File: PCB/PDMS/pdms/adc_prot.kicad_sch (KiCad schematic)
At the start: 20 parts

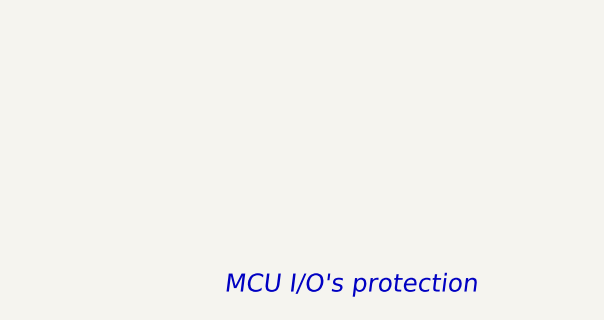
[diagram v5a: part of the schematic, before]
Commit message: WIP PCB folder structure and schematic clean-up
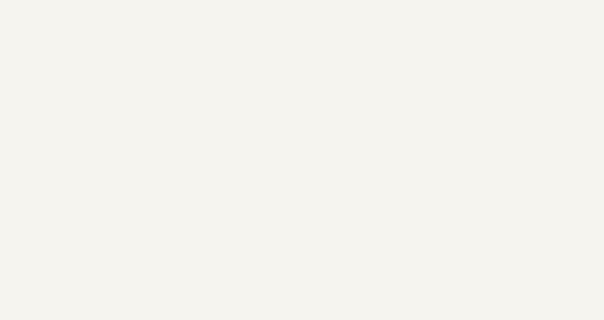
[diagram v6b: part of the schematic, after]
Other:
- note removed: "MCU I/O's protection"
- company: (none) -> PGRacing Team
- title: (none) -> MCU I/O's protection
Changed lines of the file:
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@@
 (kicad_sch (version 20211123) (generator eeschema)
   (paper "A4")
+  (title_block
+    (title "MCU I/O's protection")
+    (rev "V4.2")
+    (company "PGRacing Team")
+    (comment 1 "Karol Pergoł")
+  )
   (junction (at 125.603 107.696) (diameter 0) (color 0 0 0 0)
   )
@@
     (stroke (width 0) (type default) (color 0 0 0 0))
   )
-  (text "MCU I/O's protection" (at 186.182 191.008 0)
-    (effects (font (size 2 2) italic) (justify left bottom))
-  )
   (label "ADC_IN7" (at 106.553 129.794 0)

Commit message: PDMS PCB input modification WIP - no supply
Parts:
- added C102, C89, C96, C97: 100nF, Resistor_SMD:R_0402_1005Metric, symbol Device:C_Small
- added C32, C33, C34, C35, C36, C37, C38, C39: 47nF, Capacitor_SMD:C_0402_1005Metric, symbol Device:C_Small
- added D55, D56, D57, D58: TSD05, Diode_SMD:D_SOD-323, symbol Device:D_TVS
- added D63, D64, D65, D66: SZMM5Z5V3, Diode_SMD:D_SOD-523, symbol Device:D_Zener_Small
- added R125, R126, R129, R130, R133, R134, R135, R136: 1k/0.2W, Resistor_SMD:R_0603_1608Metric, symbol Device:R_Small
- added R127, R128, R131, R132, R137, R138, R139, R140: 100k, Resistor_SMD:R_0402_1005Metric, symbol Device:R_Small
- added U10, U11, U8, U9: MCP6002-xMC, Package_DFN_QFN:DFN-8-1EP_3x2mm_P0.5mm_EP1.75x1.45mm, symbol Amplifier_Operational:MCP6002-xMC
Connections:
- net ADC_IN1: now also D55.1 (A1), R125.1; no longer R68.2
- net ADC_IN2: now also D56.1 (A1), R126.1; no longer R70.2
- net ADC_IN3: now also D57.1 (A1), R129.1; no longer R75.2
- net ADC_IN4: now also D58.1 (A1), R130.1; no longer R77.2
- net ADC_IN5: now also R133.1; no longer R79.2
- net ADC_IN6: now also R134.1; no longer R81.2
- net ADC_IN7: now also R135.1; no longer R83.2
- net ADC_IN8: now also R136.1; no longer R85.2
- net ADC_PROT1: now also C32.1; no longer D23.6
- net ADC_PROT2: now also C33.1; no longer D23.3
- net ADC_PROT3: now also C34.1; no longer D24.6
- net ADC_PROT4: now also C35.1; no longer D24.3
- net ADC_PROT5: now also C36.1; no longer D25.6
- net ADC_PROT6: now also C37.1; no longer D25.3
- net ADC_PROT7: now also C38.1; no longer D26.6
- net ADC_PROT8: now also C39.1; no longer D26.3
- net GND: now also C102.1, C32.2, C33.2, C34.2, C35.2, C36.2, C37.2, C38.2, C39.2, C89.1, C96.1, C97.1, D55.2 (A2), D56.2 (A2), D57.2 (A2), D58.2 (A2), D63.2 (A), D64.2 (A), D65.2 (A), D66.2 (A), R127.1, R128.1, R131.1, R132.1, R137.1, R138.1, R139.1, R140.1, U10.4 (V-), U10.9 (V-), U11.4 (V-), U11.9 (V-), U8.4 (V-), U8.9 (V-), U9.4 (V-), U9.9 (V-)
- net +3.3V renamed +5V
- net +5V: now also C102.2, C89.2, C96.2, C97.2, D63.1 (K), D64.1 (K), D65.1 (K), D66.1 (K), U10.8 (V+), U11.8 (V+), U8.8 (V+), U9.8 (V+)
- new net: D26.3, R133.2, R137.2, U10.5 (+)
- new net: D24.6, R126.2, R128.2, U9.5 (+)
- new net: R75.2, U9.1, U9.2 (-)
- new net: R70.2, U9.6 (-), U9.7
- new net: D25.6, R136.2, R140.2, U10.3 (+)
- new net: R81.2, U11.6 (-), U11.7
- new net: D23.3, R129.2, R131.2, U9.3 (+)
- new net: D25.3, R135.2, R139.2, U11.3 (+)
- new net: R83.2, U11.1, U11.2 (-)
- new net: D23.6, R130.2, R132.2, U8.3 (+)
- new net: D24.3, R125.2, R127.2, U8.5 (+)
- new net: R68.2, U8.6 (-), U8.7
- new net: D26.6, R134.2, R138.2, U11.5 (+)
- new net: R85.2, U10.1, U10.2 (-)
- new net: R79.2, U10.6 (-), U10.7
- new net: R77.2, U8.1, U8.2 (-)
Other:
- moved on the sheet: D23A, D23B, D24A, D24B, D25A, D25B, D26A, D26B
